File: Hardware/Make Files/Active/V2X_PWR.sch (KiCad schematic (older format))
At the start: 39 parts, among them P1 USB_A, P11 Board Mount 2, P12 Ficudial1, P13 Board Mount 3, P14 Ficudial2, P15 Board Mount 4, P16 Ficudial3, P18 Ficudial4, P2 PG_TP, P3 Open Source, P9 Board Mount 1, U2 OKI-78SR-5, U3 PNVX002, U4 TLV70033DDC

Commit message: Saving V1.1 as archive.
We are trying a new architecture where the FTDI can be removed. making a
backup spot
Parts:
- removed C10, C11, C14, C5: 220U, Capacitors_SMD:c_elec_6.3x5.8, symbol CP
- removed C12: 10N, Capacitors_SMD:C_0603, symbol C
- removed C13: 2N7, Capacitors_SMD:C_0603, symbol C
- removed C15, C6, C8, C9: 1U, Capacitors_SMD:C_0603, symbol C
- removed C56: 4U7, Capacitors_SMD:C_0603, symbol C
- removed C?: 1U, symbol C
- removed FB2, FB3: 220, Capacitors_SMD:C_0805, symbol FILTER
- removed FB?: FILTER, symbol FILTER
- removed P2: PG_TP, Measurement_Points:Measurement_Point_Round-SMD-Pad_Small, symbol CONN_01X01
- removed P?: USB_u, Connect:USB_Micro-B, symbol USB_OTG
- removed R4: 220, Resistors_SMD:R_0603, symbol R
- removed R5: 1K7, Resistors_SMD:R_0603, symbol R
- removed U2: OKI-78SR-5, Custom Parts:TO-220_OKI-78SR, symbol OKI-78SR
- removed U3: PNVX002, Custom Parts:PNVX002, symbol PNVX002
- removed U4: TLV70033DDC, Housings_SOT-23_SOT-143_TSOT-6:SOT-23-5, symbol TLV70033DDC
- added C46, C49, C53: 4U7, Capacitors_SMD:C_1210, symbol C
- added C47: 220P, Capacitors_SMD:C_1210, symbol C
- added C48, C51, C52, C55: 10U, Capacitors_SMD:C_1210, symbol C
- added C54: 560P, Capacitors_SMD:C_1210, symbol C
- added D12, D14, D15: PMEG3030, symbol D_Schottky_Small
- added D13: 1V8, symbol ZENER
- added JP1, JP2, JP3: JUMPER, symbol JUMPER
- added L3, L4: 5U6, symbol INDUCTOR_SMALL
- added L5: 12U, symbol INDUCTOR_SMALL
- added P?: USB_u, Connect:USB_Micro-B, symbol USB_OTG
- added Q11, Q12, Q14: IRF9335, symbol Q_PMOS_GSD
- added Q13: BSS84, symbol Q_PMOS_GSD
- added Q15: 2N7000, symbol Q_NMOS_GSD
- added R57, R60, R62, R64, R67, R71: 2K0, symbol R
- added R58, R66, R? (x2): 0, symbol R
- added R59, R69: 10K5, symbol R
- added R61: 8K2, symbol R
- added R63, R70: 47K, symbol R
- added R65: 10.5K, symbol R
- added R68: 6K2, symbol R
- added SW2: SW_PUSH, symbol SW_PUSH
- added U11, U13, U14: XRP6124, symbol XRP6124
- added U12, U15, U? (x2): SLG59M, symbol SLG59M
- C50: renamed from C7; value 33U -> 330P
- renumbered C3 to C44, C4 to C45, D1 to D10, D2 to D11, P14 to P10, P16 to P12, P18 to P14, P1 to P6, P12 to P7, P3 to P8
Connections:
- net labels added: 12V0_A, 12V0_B, 3V3_A, 3V3_B, 3V3_B_EN, 3V3_C, 3V3_C_EN, 3V3_D, 3V3_D_EN, 3V3_EN, 4V1_A, 4V1_EN, 5V0_A, 5V0_B, 5V0_B_EN, 5V0_B_OUT, 5V0_EN, BUTTON, HUB_DM, HUB_DP
- net labels removed: 12V0, 12V0RAW, 3V3, 3V3_ADC, 3V3_CONST, 4V1, 4V1F1, 5V0, 5V0_OUT, FTDI_RESET, PD0, USB_M, USB_P
- wire segments 23 -> 91
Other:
- note added: "3.3V @ 1A DC-DC Power Supply"
- note added: "4.1V @ 1.5A DC-DC Power Supply"
- note added: "5V @ 1.25A DC-DC Power Supply"
- note added: "Accelerometer 3V3 rail"
- note added: "Button force starts the 3V3 to start PWRSEQ\nPWRSEQ must hold pin high to stay on\nButton acts soft button once running"
- note added: "CAN 3V3 rail"
- note added: "HUB & FTDI 3V3 rail"
- note added: "HUB Data, HOST Power"
- note added: "PWRSEQ will siphon power from 4V1\nand disable the 3V3 Supply while \nin Cell standby recieve power state."
- note added: "Slew Rate is\nControlable"
- note removed: "3.3V @ 1.5A DC-DC Power Supply"
- note removed: "4.1V @ 2A DC-DC Power Supply"
- note removed: "5V @ 1.5A DC-DC Power Supply"
- note removed: "HOST Data/Power Connection"
- moved on the sheet: C44, C45, C50, D10, D11, F1, F2, P10, P11, P12, P13, P14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

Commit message: V1.2 mostly done
BOM is integrated and creates mouser orders
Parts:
- removed C46, C49: 4U7, Capacitors_SMD:C_1210, symbol C
- removed C51: 10U, Capacitors_SMD:C_1210, symbol C
- removed D15: PMEG3030, symbol D_Schottky_Small
- removed JP1, JP2, JP3: JUMPER, symbol JUMPER
- removed Q15: 2N7000, symbol Q_NMOS_GSD
- removed R57: 2K0, symbol R
- removed R58, R? (x2): 0, symbol R
- removed U13: XRP6124, symbol XRP6124
- removed U? (x2): SLG59M, symbol SLG59M
- added C47, C50: 4U7, Capacitors_SMD:C_0603, symbol C
- added C56: 10U, Capacitors_SMD:C_1210, symbol C
- added D14: SBR3U30P1-7, symbol D_Schottky_Small
- added P17, P18, P19: NVM_RST, Connect:PINHEAD1-2, symbol CONN_01X02
- added Q15: 2N7000, symbol Q_NMOS_SGD
- added R72: 6K2, Resistors_SMD:R_0603, symbol R
- added R73: 10.5K, Resistors_SMD:R_0603, symbol R
- added R74: 47K, Resistors_SMD:R_0603, symbol R
- added R75: 2K0, Resistors_SMD:R_0603, symbol R
- added R76: 0, Resistors_SMD:R_0603, symbol R
- added U13, U16, U18: SLG59M, symbol SLG59M
- added U14: XRP6124, symbol XRP6124
- C45: renamed from C44; Mouse PN (none) -> 77-VJ0603Y103KXACBC
- C46: renamed from C45; Mouse PN (none) -> 667-EEE-FT1V101AP
- C48: renamed from C47; Mouse PN (none) -> 581-06035A221J
- C49: renamed from C48; Mouse PN (none) -> 603-CC126KKX7R7BB106
- C51: renamed from C50; Mouse PN (none) -> 80-C0603C331J5G
- C52: Mouse PN (none) -> 603-CC126KKX7R7BB106
- C53: value 4U7 -> 10U; Mouse PN (none) -> 603-CC126KKX7R7BB106
- C54: value 560P -> 4U7; footprint Capacitors_SMD:C_1210 -> Capacitors_SMD:C_0603; Mouse PN (none) -> 581-12063C475KAT2A
- C55: value 10U -> 560P; footprint Capacitors_SMD:C_1210 -> Capacitors_SMD:C_0603; Mouse PN (none) -> 77-VJ0603Y561KXACBC
- D10: value DB2441700L -> B320A-13-F; Mouse PN (none) -> 621-B320A-F
- D11: Mouse PN (none) -> 576-SD15C-01FTG
- D12: value PMEG3030 -> SBR3U30P1-7; Mouse PN (none) -> 621-SBR3U30P1-7
- D13: renamed from D14; value PMEG3030 -> SBR3U30P1-7; Mouse PN (none) -> 621-SBR3U30P1-7
- D15: renamed from D13; Mouse PN (none) -> 863-MMSZ4678T1G
- F1: value 2A -> 1.1A; Mouse PN (none) -> 530-0ZCG0110AF2C
- F2: Mouse PN (none) -> 530-0ZCC0125FF2C
- L3, L4: Mouse PN (none) -> 652-SRP4020TA-5R6M
- L5: value 12U -> 10U; Mouse PN (none) -> 652-SRP4020TA-100M
- P14: renamed from P6; Mouse PN (none) -> 571-6364372-2
- P9: renamed from P?; Mouse PN (none) -> 656-DX4R005JJ2R1800
- Q11, Q12, Q14: Mouse PN (none) -> 942-IRF9335TRPBF
- Q13: footprint (none) -> Housings_SOT-23_SOT-143_TSOT-6:SOT-23; Mouse PN (none) -> 512-BSS84
- R59: value 10K5 -> 0; footprint (none) -> Resistors_SMD:R_0603; Mouse PN (none) -> 71-CRCW0603-0-E3
- R60, R67: value 2K0 -> 0; footprint (none) -> Resistors_SMD:R_0603; Mouse PN (none) -> 71-CRCW0603-0-E3
- R61: value 8K2 -> 2K0; footprint (none) -> Resistors_SMD:R_0603; Mouse PN (none) -> 71-CRCW0603-2.0k-E3
- R62: value 2K0 -> 10.5K; footprint (none) -> Resistors_SMD:R_0603; Mouse PN (none) -> 71-CRCW0603-10.5k-E3
- R63: value 47K -> 2K0; footprint (none) -> Resistors_SMD:R_0603; Mouse PN (none) -> 71-CRCW0603-2.0k-E3
- R64: value 2K0 -> 8K2; footprint (none) -> Resistors_SMD:R_0603; Mouse PN (none) -> 71-CRCW0603-8.2K-E3
- R65: value 10.5K -> 2K0; footprint (none) -> Resistors_SMD:R_0603; Mouse PN (none) -> 71-CRCW0603-2.0k-E3
- R66: value 0 -> 47K; footprint (none) -> Resistors_SMD:R_0603; Mouse PN (none) -> 71-CRCW0603-47k-E3
- R68: value 6K2 -> 0; footprint (none) -> Resistors_SMD:R_0603; Mouse PN (none) -> 71-CRCW0603-0-E3
- R69: value 10K5 -> 2K0; footprint (none) -> Resistors_SMD:R_0603; Mouse PN (none) -> 71-CRCW0603-2.0k-E3
- R70: value 47K -> 10.5K; footprint (none) -> Resistors_SMD:R_0603; Mouse PN (none) -> 71-CRCW0603-10.5k-E3
- R71: footprint (none) -> Resistors_SMD:R_0603; Mouse PN (none) -> 71-CRCW0603-2.0k-E3
- SW2: Mouse PN (none) -> 506-FSMSM
- U11: Mouse PN (none) -> 701-XRP6124ESTR0.5-F
- U12, U15: Mouse PN (none) -> 402-SLG59M1440V
- U17: renamed from U14; Mouse PN (none) -> 701-XRP6124ESTR0.5-F
- renumbered P11 to P10, P10 to P11, P13 to P12, P12 to P13, P14 to P16, P9 to P6
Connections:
- net labels added: 5V0_C, 5V0_C_EN
- wire segments 91 -> 60
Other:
- note added: "Button force starts the 3V3 to start SEQ\nSEQ must hold 3V3_EN high to stay on\nBUTTON is soft button signal once running\n3V3_EN pulled low kills supply regaurdless if button pressed"
- note added: "CAN 5V0 rail"
- note added: "HOST 5V0 rail"
- note removed: "Button force starts the 3V3 to start PWRSEQ\nPWRSEQ must hold pin high to stay on\nButton acts soft button once running"
- moved on the sheet: C45, C46, D10, D11, D15, F1, F2, P10, P11, P12, P13, P14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

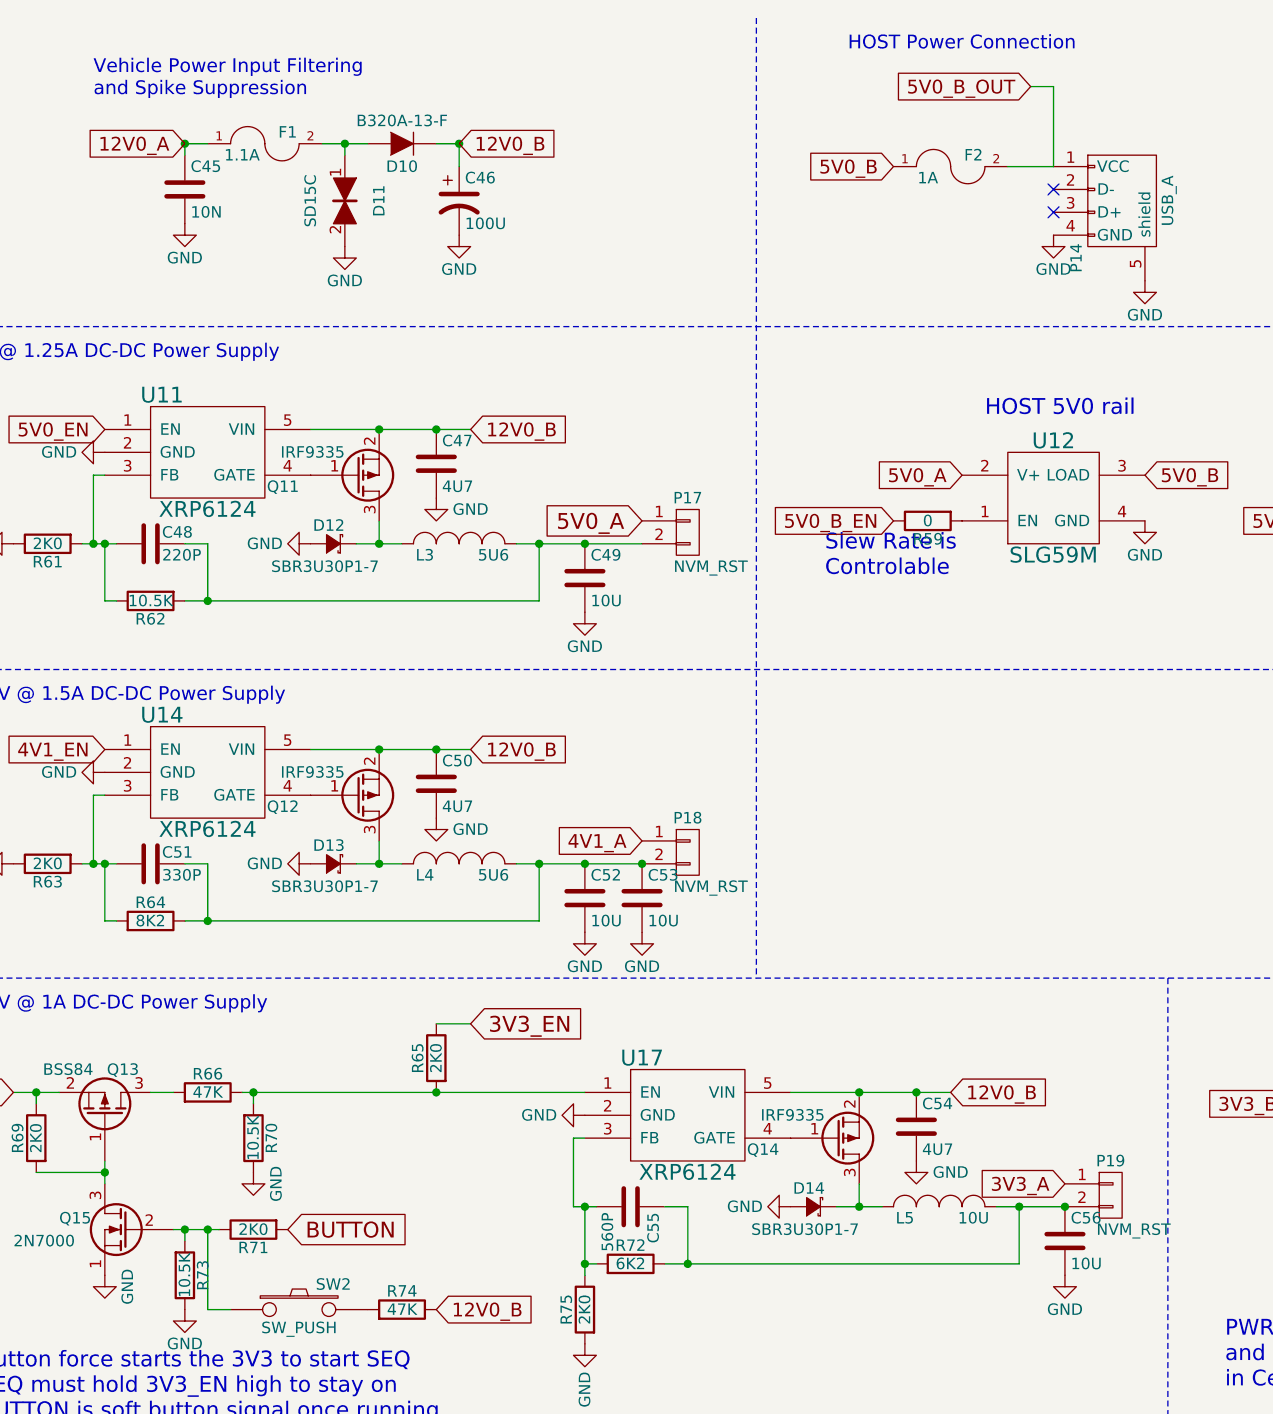
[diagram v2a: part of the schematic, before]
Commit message: V2X v1.2 sch and bom
Made changes to the schematic to V1.2 (remove FTDI possibly) and
integrade the BOM information into the sch
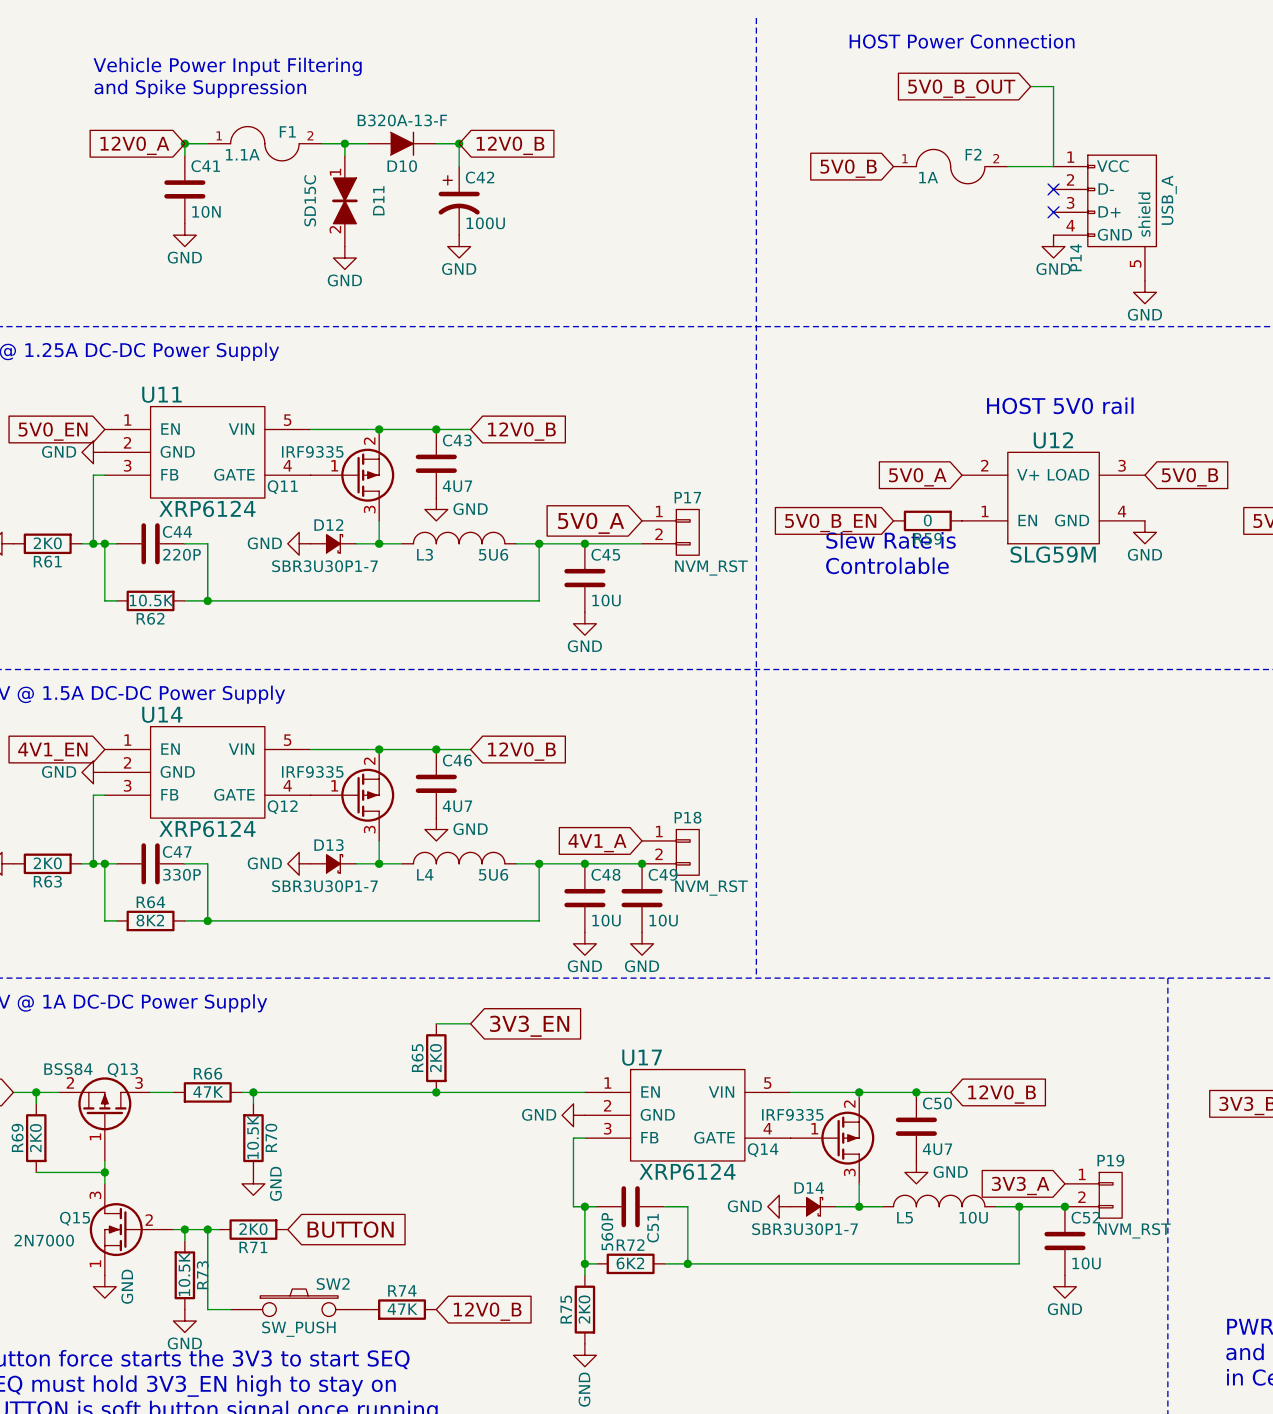
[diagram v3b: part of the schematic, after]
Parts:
- renumbered C45 to C41, C46 to C42, C47 to C43, C48 to C44, C49 to C45, C50 to C46, C51 to C47, C52 to C48, C53 to C49, C54 to C50, C55 to C51, C56 to C52
